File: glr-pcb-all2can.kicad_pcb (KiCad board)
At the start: 4 copper layers, 64 x 40 mm, 91 parts, among them IC1 ATA6561-GAQW-N, IC2 ZMR330FTA, IC3 AP64060WU-7, IC4 STM32C092KCT6, IC5 LSM6DSV16BXTR, J1 DA15_Pins_MountingHoles, J3 Conn_01x04, J4 Conn_01x02, J5 Conn_01x02, J6 62701021621, Q1 DMN6075S, Q2 DMN6075S, Q3 DMN6075S, Q4 DMN6075S

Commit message: finish routing everything
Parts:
- moved G*** 0.71 mm to (161.1, 126.1)
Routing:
- net /Input filter/6_IN: track 5.64 -> 31.2 mm, vias 2 -> 1
- net /Output/4_OUT: track 8.88 -> 26.2 mm, vias 0 -> 2
- net /Input filter/2_IN: track 14.6 -> 23.2 mm, vias 2 -> 4
- net /Input filter/3_IN: track 31.9 -> 35.9 mm, vias 4 -> 3
- net /Output/3_OUT: track 31.7 -> 33.5 mm, vias 3 -> 1
- net GND: track 144.5 -> 145.6 mm
- net /Input filter/1_IN: track 25.5 -> 24.4 mm, vias 6 -> 5
- net /Output/1_OUT: track 51.6 -> 52.3 mm

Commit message: remove inner layers
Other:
- copper layers 4 -> 2
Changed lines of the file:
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@@
 	(layers
 		(0 "F.Cu" signal)
-		(4 "In1.Cu" signal)
-		(6 "In2.Cu" signal)
 		(2 "B.Cu" signal)
 		(9 "F.Adhes" user "F.Adhesive")
@@
 			)
 			(layer "dielectric 1"
-				(type "prepreg")
-				(thickness 0.1)
-				(material "FR4")
-				(epsilon_r 4.5)
-				(loss_tangent 0.02)
-			)
-			(layer "In1.Cu"
-				(type "copper")
-				(thickness 0.035)
-			)
-			(layer "dielectric 2"
 				(type "core")
-				(thickness 1.24)
-				(material "FR4")
-				(epsilon_r 4.5)
-				(loss_tangent 0.02)
-			)
-			(layer "In2.Cu"
-				(type "copper")
-				(thickness 0.035)
-			)
-			(layer "dielectric 3"
-				(type "prepreg")
-				(thickness 0.1)
+				(thickness 1.51)
 				(material "FR4")
 				(epsilon_r 4.5)
@@
 		(pcbplotparams
 			(layerselection 0x00000000_00000000_55555555_5755f5ff)
-			(plot_on_all_layers_selection 0x00000000_00000000_00000000_00000000)
+			(plot_on_all_layers_selection 0x00000000_00000000_00000000_00000005)
 			(disableapertmacros no)
 			(usegerberextensions no)
@@
 			(psnegative no)
 			(psa4output no)
-			(plot_black_and_white yes)
+			(plot_black_and_white no)
 			(sketchpadsonfab no)
 			(plotpadnumbers no)
@@
 			(crossoutdnponfab yes)
 			(subtractmaskfromsilk no)
-			(outputformat 1)
+			(outputformat 4)
 			(mirror no)
-			(drillshape 1)
+			(drillshape 0)
 			(scaleselection 1)
-			(outputdirectory "")
+			(outputdirectory "output/")
 		)
 	)
@@
 			(at 4.315 14.73 0)
 			(layer "F.Fab")
+			(hide yes)
 			(effects
 				(font

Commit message: add my self :)
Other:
- board text added: "${COMPANY} ${TITLE} ${PROJECTNAME} ${REVISION} ${ISSUE_DATE} ${COMMENT1} ${COMMENT2} ${COMMENT3}"
- board text removed: "${COMPANY} ${TITLE} ${PROJECTNAME} ${REVISION} ${ISSUE_DATE}"
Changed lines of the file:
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@@
 		(layer "Edge.Cuts")
 	)
-	(gr_text "${COMPANY}\n${TITLE}\n${PROJECTNAME} ${REVISION}\n${ISSUE_DATE}"
-		(at 173.7 96.93 0)
+	(gr_text "${COMPANY}\n${TITLE}\n${PROJECTNAME} ${REVISION}\n${ISSUE_DATE}\n${COMMENT1}\n${COMMENT2}\n${COMMENT3}"
+		(at 173.77 91.11 0)
 		(layer "B.SilkS")
 		(effects
@@
 				(thickness 0.125)
 			)
-			(justify left bottom mirror)
+			(justify left top mirror)
 		)
 	)

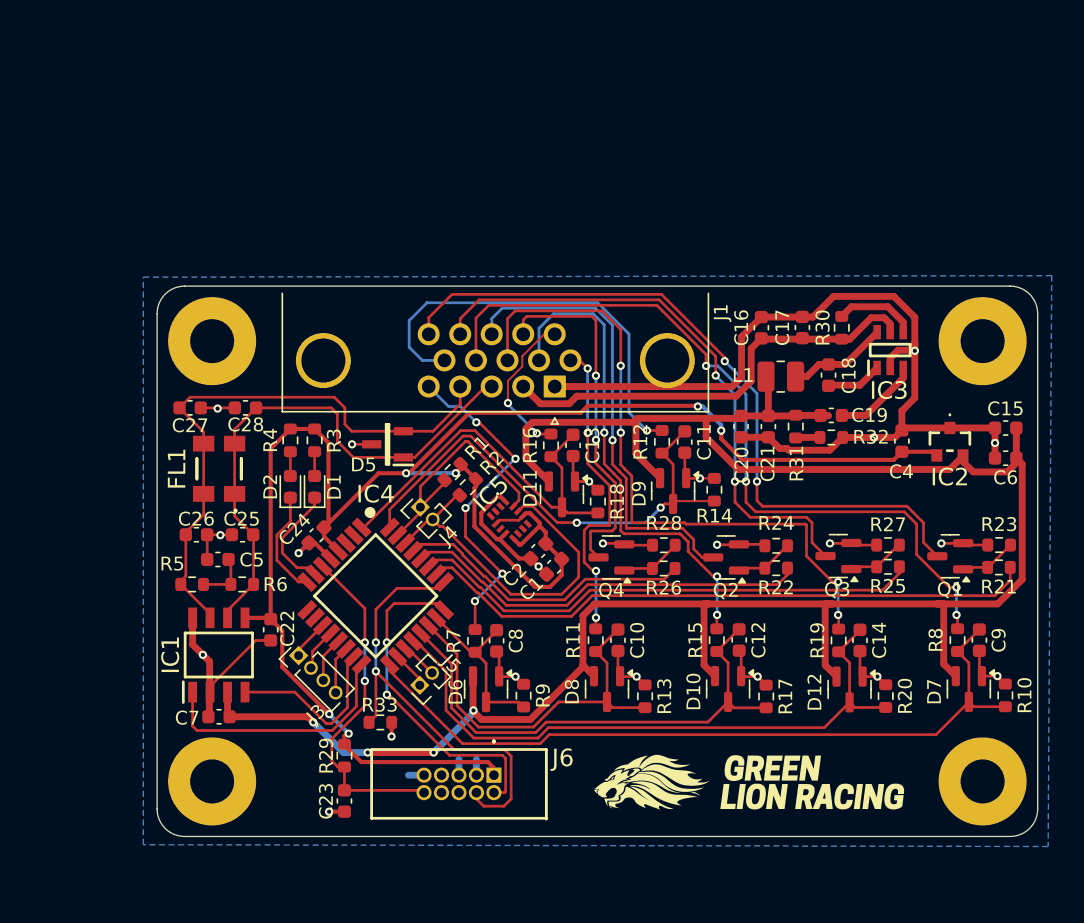
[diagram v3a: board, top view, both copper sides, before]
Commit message: massive overhaul of pcb
* replace sub-d with 4x m12a 4pin circular connector
* fit board to bopla bolink case
* restructure entire board
* add second main voltage converter for powering input devices
* reduce inputs to 5
* remove 6 axis imu
* remove outputs
* remove mounting holes
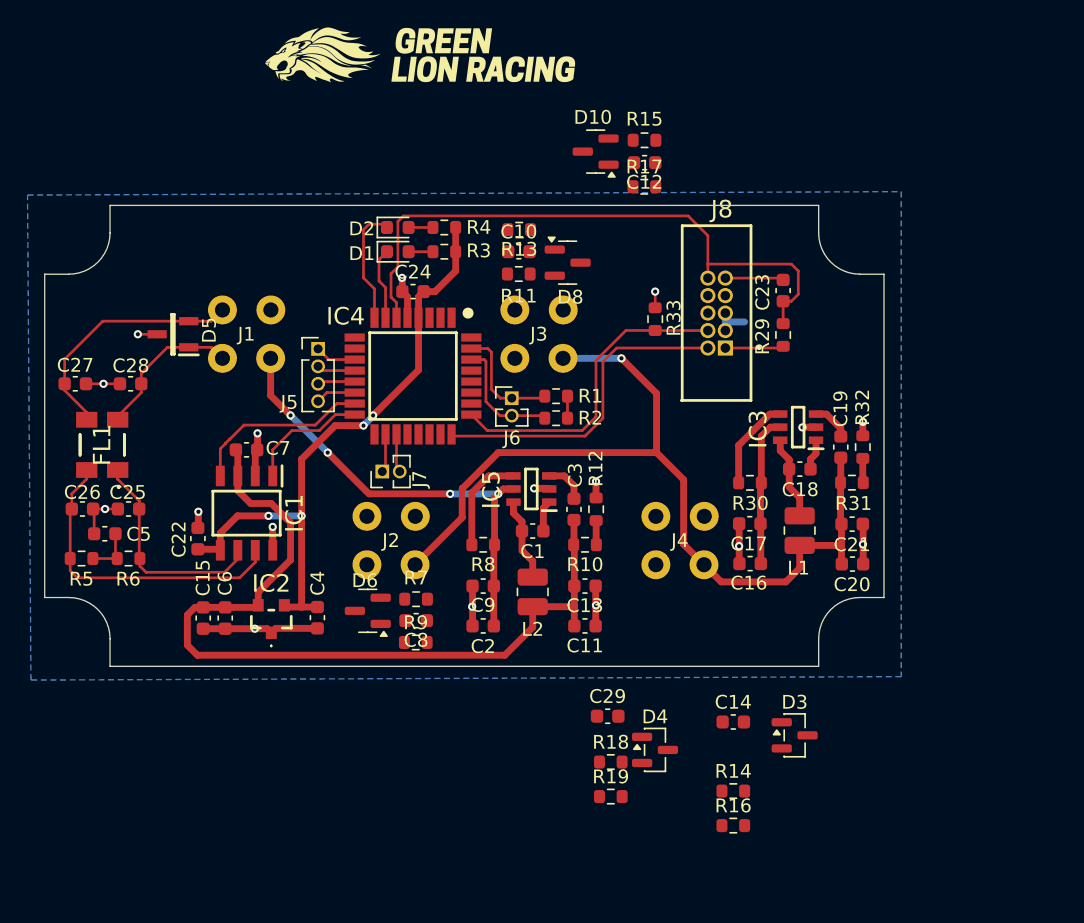
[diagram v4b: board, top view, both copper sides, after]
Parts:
- removed D11, D12, D7, D9: BAT54S, Package_TO_SOT_SMD:SOT-23
- removed Q1, Q2, Q3, Q4: DMN6075S, Package_TO_SOT_SMD:SOT-23
- removed R20: ~, Resistor_SMD:R_0603_1608Metric
- removed R21, R22, R25, R26: 200, Resistor_SMD:R_0603_1608Metric
- removed R23, R24, R27, R28: 10k, Resistor_SMD:R_0603_1608Metric
- removed REF** (x4): MountingHole_3.2mm_M3_Pad, MountingHole:MountingHole_3.2mm_M3_Pad
- added C29: 100n, Capacitor_SMD:C_0603_1608Metric, F.Cu at (150.8, 121.3)
- added C3: 100n, Capacitor_SMD:C_0603_1608Metric, F.Cu at (148.3, 106.2)
- added D3: BAT54S, Package_TO_SOT_SMD:SOT-23, F.Cu at (164.3, 122.7)
- added D4: BAT54S, Package_TO_SOT_SMD:SOT-23, F.Cu at (154.2, 123.7)
- added J2: Conn_02x02_Counter_Clockwise_Shielded, GLR_KiCad_Library:M12A-04P, F.Cu at (135.0, 108.5)
- added J3: Conn_02x02_Counter_Clockwise_Shielded, GLR_KiCad_Library:M12A-04P, F.Cu at (145.8, 93.5)
- added J4: Conn_02x02_Counter_Clockwise_Shielded, GLR_KiCad_Library:M12A-04P, F.Cu at (156.0, 108.5)
- added L2: 10u, Inductor_SMD:L_1008_2520Metric, F.Cu at (145.3, 112.2)
- C11: value 100n -> 1u
- C2: value 100n -> 2u2
- IC5: value LSM6DSV16BXTR -> AP64060WU-7; footprint SamacSys_Parts:LSM6DSV16BXTR -> SamacSys_Parts:SOT95P280X100-6N
- J1: value DA15_Pins_MountingHoles -> Conn_02x02_Counter_Clockwise_Shielded; footprint Connector_Dsub:DSUB-15-HD_Pins_Horizontal_P2.29x1.90mm_EdgePinOffset3.03mm_Housed_MountingHolesOffset4.94mm -> GLR_KiCad_Library:M12A-04P
- R10: value ~ -> 51
- R12: value 30k -> 10
- R14, R18: value ~ -> 30k
- R16, R19: value 30k -> ~
- R8: value 30k -> 10k
- moved C15 59.9 mm to (121.3, 114.1), turned to -90 degrees
- moved G*** 58.0 mm to (137.2, 73.2)
- moved C6 57.9 mm to (123.0, 114.1), turned to -90 degrees
- moved IC2 51.0 mm to (126.3, 114.2), turned to 180 degrees
- moved C23 48.9 mm to (163.5, 90.3), turned to -90 degrees
- moved C4 44.4 mm to (129.7, 114.1), turned to 90 degrees
- moved R29 44.2 mm to (163.5, 93.5), turned to 90 degrees
- moved D10 40.2 mm to (149.9, 80.2), turned to 180 degrees
- moved R17 38.1 mm to (153.4, 82.8), turned to 0 degrees
- moved R15 36.7 mm to (153.4, 79.4), turned to 180 degrees
- moved C9 36.3 mm to (141.7, 111.8), turned to 180 degrees
- moved R33 35.5 mm to (154.2, 92.4), turned to 90 degrees
- moved C12 35.4 mm to (153.4, 81.0), turned to 180 degrees
- moved J8 35.3 mm to (159.3, 94.5), turned to 90 degrees
- moved R8 35.2 mm to (141.7, 108.8), turned to 0 degrees
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- renumbered J3 to J5, J4 to J6, J5 to J7, J6 to J8
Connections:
- C1 pad 1: GND -> Net-(IC5-BST)
- C1 pad 2: +3V3 -> Net-(IC5-SW)
- C11 pad 1: IC_IN_6 -> GND
- C11 pad 2: GND -> +5V
- C13 pad 1: IC_IN_7 -> GND
- C13 pad 2: GND -> +5V
- C19 pad 2: +5V -> +XXV
- C2 pad 1: +3V3 -> +24V
- C20 pad 2: +5V -> +XXV
- C21 pad 2: +5V -> +XXV
- C25 pad 1: /CAN transciever/CAN L 1 -> Net-(IC1-CANL)
- C26 pad 2: /CAN transciever/CAN H 1 -> Net-(IC1-CANH)
- C9 pad 1: IC_IN_5 -> +24V
- FL1 pad 1: /CAN transciever/CAN L 1 -> Net-(IC1-CANL)
- FL1 pad 4: /CAN transciever/CAN H 1 -> Net-(IC1-CANH)
- IC1 pad 6: /CAN transciever/CAN L 1 -> Net-(IC1-CANL)
- IC1 pad 7: /CAN transciever/CAN H 1 -> Net-(IC1-CANH)
- IC4 pad 1: IC_IN_7 -> unconnected-(IC4-PB9-Pad1)
- IC4 pad 17: IC_IN_5 -> unconnected-(IC4-PB2-Pad17)
- IC4 pad 20: IC_IN_4 -> unconnected-(IC4-PC6-Pad20)
- IC4 pad 26: IC_OUT_1 -> unconnected-(IC4-PA15-Pad26)
- IC4 pad 27: IC_OUT_2 -> unconnected-(IC4-PB3-Pad27)
- IC4 pad 28: IC_OUT_3 -> unconnected-(IC4-PB4-Pad28)
- IC4 pad 29: IC_OUT_4 -> unconnected-(IC4-PB5-Pad29)
- IC4 pad 32: IC_IN_6 -> unconnected-(IC4-PB8-Pad32)
- IC5 pad 1: GND -> Net-(IC5-BST)
- IC5 pad 2: unconnected-(IC5-TDMOUT-Pad2) -> GND
- IC5 pad 3: unconnected-(IC5-BCLK-Pad3) -> Net-(IC5-FB)
- IC5 pad 4: unconnected-(IC5-INT1-Pad4) -> Net-(IC5-EN)
- IC5 pad 5: +3V3 -> +24V
- IC5 pad 6: unconnected-(IC5-AH1/QVAR1-Pad6) -> Net-(IC5-SW)
- J1 pad 2: +24V -> /CAN transciever/CAN H 1
- J1 pad 4: /CAN transciever/CAN H 1 -> +24V
- L1 pad 2: +5V -> +XXV
- R10 pad 1: GND -> +5V
- R10 pad 2: IC_IN_5 -> Net-(R10-Pad2)
- R12 pad 1: /Input filter/6_IN -> Net-(R10-Pad2)
- R12 pad 2: IC_IN_6 -> GND
- R14 pad 1: GND -> /Input filter/4_IN
- R14 pad 2: IC_IN_6 -> IC_IN_4
- R16 pad 1: /Input filter/7_IN -> GND
- R16 pad 2: IC_IN_7 -> IC_IN_4
- R18 pad 1: GND -> /Input filter/5_IN
- R18 pad 2: IC_IN_7 -> IC_IN_5
- R19 pad 1: /Input filter/4_IN -> GND
- R19 pad 2: IC_IN_4 -> IC_IN_5
- R31 pad 1: +5V -> +XXV
- R5 pad 2: /CAN transciever/CAN H 1 -> Net-(IC1-CANH)
- R6 pad 1: /CAN transciever/CAN L 1 -> Net-(IC1-CANL)
- R8 pad 1: /Input filter/5_IN -> Net-(IC5-EN)
- R8 pad 2: IC_IN_5 -> +24V
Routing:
- net +5V: track 163.3 -> 60.8 mm, vias 4 -> 0
- net GND: track 145.6 -> 48.9 mm, vias 22 -> 17
- net +3V3: track 131.4 -> 51.6 mm, vias 6 -> 4
- net +XXV: track 0.00 -> 64.2 mm, vias 0 -> 1
- net /Input filter/5_IN: track 56.3 -> 0.00 mm, vias 4 -> 0
- net IC_IN_5: track 55.1 -> 0.00 mm
- net /Output/1_OUT: track 52.3 -> 0.00 mm, vias 2 -> 0
- net /Input filter/4_IN: track 48.0 -> 0.00 mm, vias 4 -> 0
- net IC_IN_4: track 46.4 -> 0.00 mm
- net IC_OUT_1: track 45.4 -> 0.00 mm
- net /Output/2_OUT: track 42.2 -> 0.00 mm, vias 2 -> 0
- net IC_OUT_2: track 37.6 -> 0.00 mm
- net IC_IN_3: track 37.4 -> 0.00 mm
- net IC_IN_6: track 36.7 -> 0.00 mm, vias 2 -> 0
- net /Input filter/3_IN: track 35.9 -> 0.00 mm, vias 3 -> 0
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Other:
- board size 64 x 40 mm -> 61 x 33.5 mm

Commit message: update buck converters
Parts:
- removed C18, C19, C21: 100n, Capacitor_SMD:C_0603_1608Metric
- removed C20: 1u, Capacitor_SMD:C_0603_1608Metric
- removed IC3: AP64060WU-7, SamacSys_Parts:SOT95P280X100-6N
- removed L1: 10u, Inductor_SMD:L_1008_2520Metric
- removed R30: 10k, Resistor_SMD:R_0603_1608Metric
- removed R31: 51, Resistor_SMD:R_0603_1608Metric
- removed R32: 10, Resistor_SMD:R_0603_1608Metric
- added C30: 2u2, Capacitor_SMD:C_0603_1608Metric, F.Cu at (140.4, 128.6)
- added C31: 2u2, Capacitor_SMD:C_0603_1608Metric, F.Cu at (179.4, 105.7)
- added IC6: AP64060WU-7, SamacSys_Parts:SOT95P280X100-6N, F.Cu at (176.3, 109.4)
- added L3: ~, Inductor_SMD:L_1008_2520Metric, F.Cu at (174.4, 105.2)
- added R20: 10k, Resistor_SMD:R_0603_1608Metric, F.Cu at (177.8, 105.7)
- added R21: ~, Resistor_SMD:R_0603_1608Metric, F.Cu at (179.0, 111.7)
- added R22: 22.1k, Resistor_SMD:R_0603_1608Metric, F.Cu at (176.6, 112.4)
- C16: value 2u2 -> 1u
- C2: value 2u2 -> 100n
- R10: value 51 -> 22.1k
- R12: value 10 -> 115k
- moved C9 38.9 mm to (180.6, 111.7), turned to -90 degrees
- moved C2 32.5 mm to (173.7, 108.8), turned to 90 degrees
- moved C13 21.1 mm to (141.3, 131.4)
- moved IC5 20.3 mm to (143.2, 124.9), turned to -90 degrees
- moved C11 20.0 mm to (141.3, 133.1)
- moved R8 19.8 mm to (142.1, 128.6), turned to 90 degrees
- moved C16 19.6 mm to (178.6, 101.3), turned to 0 degrees
- moved C3 19.0 mm to (139.1, 122.8), turned to 90 degrees
- moved R12 19.0 mm to (140.7, 122.8)
- moved C17 18.0 mm to (178.6, 103.0), turned to 0 degrees
- moved C1 17.9 mm to (146.0, 125.6), turned to -90 degrees
- moved L2 17.0 mm to (145.4, 129.2)
- moved R10 14.6 mm to (143.0, 122.0), turned to 180 degrees
- moved C14 1.75 mm to (161.6, 121.7)
- moved C29 1.75 mm to (152.5, 121.3)
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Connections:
- C11 pad 1: GND -> +5V
- C11 pad 2: +5V -> GND
- C13 pad 1: GND -> +5V
- C13 pad 2: +5V -> GND
- C16 pad 1: +24V -> +XXV
- C17 pad 1: +24V -> +XXV
- C2 pad 1: +24V -> Net-(IC6-BST)
- C2 pad 2: GND -> Net-(IC6-SW)
- C3 pad 1: Net-(IC5-FB) -> +5V
- C3 pad 2: +5V -> Net-(IC5-FB)
- C9 pad 1: +24V -> +XXV
- C9 pad 2: GND -> Net-(IC6-FB)
- D10 pad 2: +5V -> +3V3
- D3 pad 2: +5V -> +3V3
- D4 pad 2: +5V -> +3V3
- D6 pad 2: +5V -> +3V3
- D8 pad 2: +5V -> +3V3
- R10 pad 1: +5V -> GND
- R10 pad 2: Net-(R10-Pad2) -> Net-(IC5-FB)
- R12 pad 1: Net-(R10-Pad2) -> +5V
- R12 pad 2: GND -> Net-(IC5-FB)
- R8 pad 1: Net-(IC5-EN) -> +24V
- R8 pad 2: +24V -> Net-(IC5-EN)
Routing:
- net +5V: track 60.8 -> 44.7 mm
- net GND: track 48.9 -> 63.0 mm, vias 17 -> 9
- net +24V: track 44.1 -> 30.4 mm, vias 4 -> 2
- net Net-(IC5-EN): track 7.31 -> 0.00 mm
- net Net-(IC3-EN): track 6.69 -> 0.00 mm
- net Net-(IC3-SW): track 6.08 -> 0.00 mm
- net Net-(IC6-FB): track 0.00 -> 5.00 mm
- net Net-(IC6-SW): track 0.00 -> 4.28 mm
- net Net-(IC3-FB): track 2.81 -> 0.00 mm
- net Net-(IC3-BST): track 2.27 -> 0.00 mm
- net Net-(IC6-BST): track 0.00 -> 2.17 mm
- net +XXV: track 64.2 -> 66.2 mm
- net Net-(IC6-EN): track 0.00 -> 1.78 mm
- net Net-(R31-Pad2): track 1.77 -> 0.00 mm
- net Net-(IC5-FB): track 3.04 -> 4.80 mm
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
